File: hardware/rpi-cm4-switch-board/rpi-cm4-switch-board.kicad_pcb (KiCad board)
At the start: 2 copper layers, 114.5 x 102 mm, 68 parts, among them J1 0826-1G1T-23-F, J2 0826-1G1T-23-F, J3 0826-1G1T-23-F, P1 USB_C_Plug_USB2.0, P2 USB_C_Plug_USB2.0, U3 74LVC1G07SE-7, U5 KSZ9567RTXI, U6 AP2127N-2.5, U7 AP2127N3-1.2

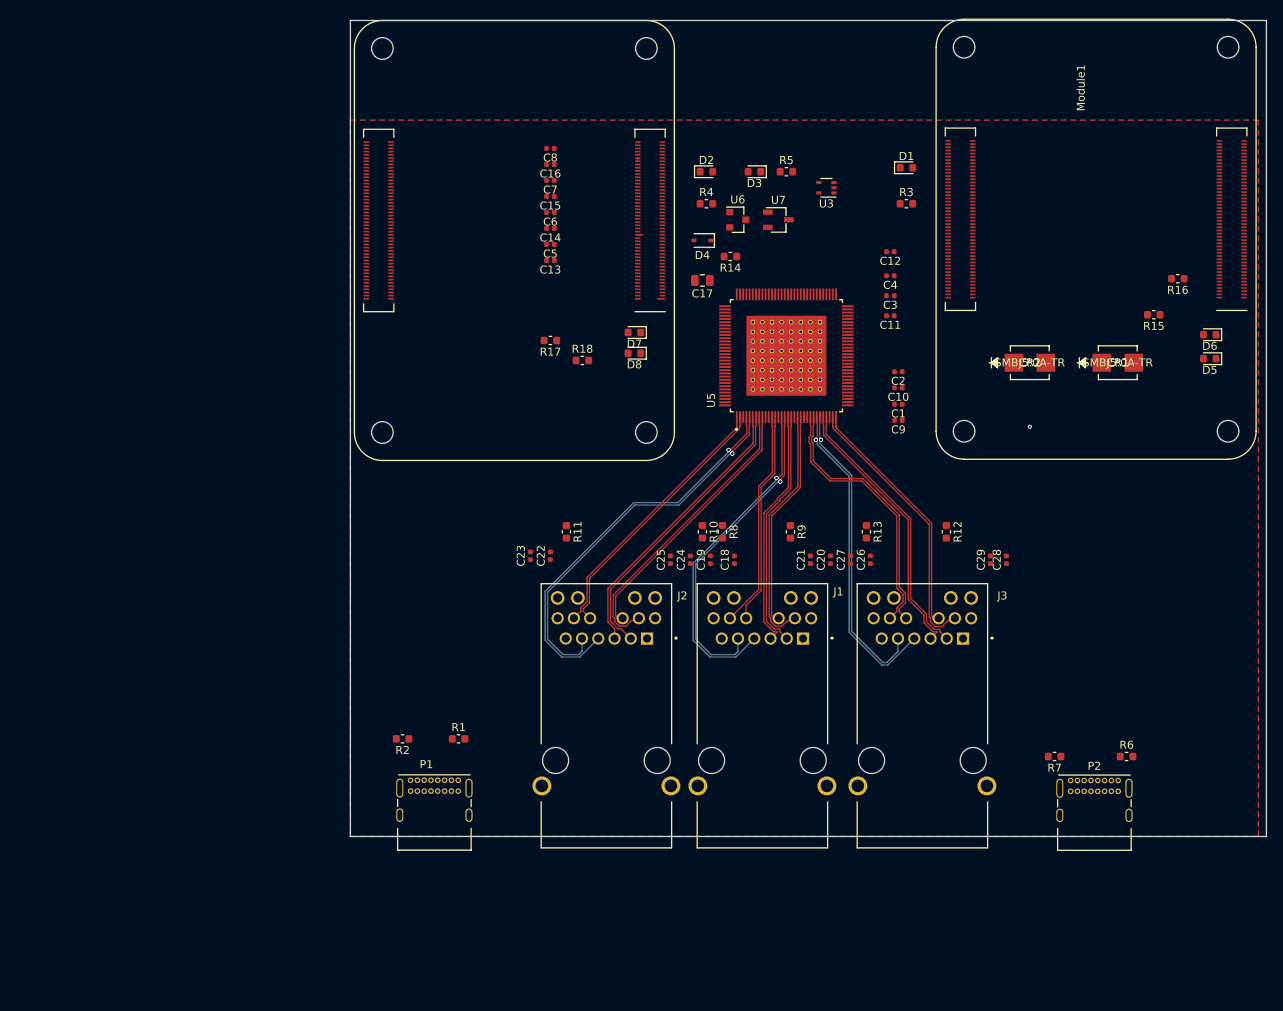
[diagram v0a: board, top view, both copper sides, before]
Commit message: Differential routing completed/roughed out. Schematic cleanup. More work to do on chip power pins.
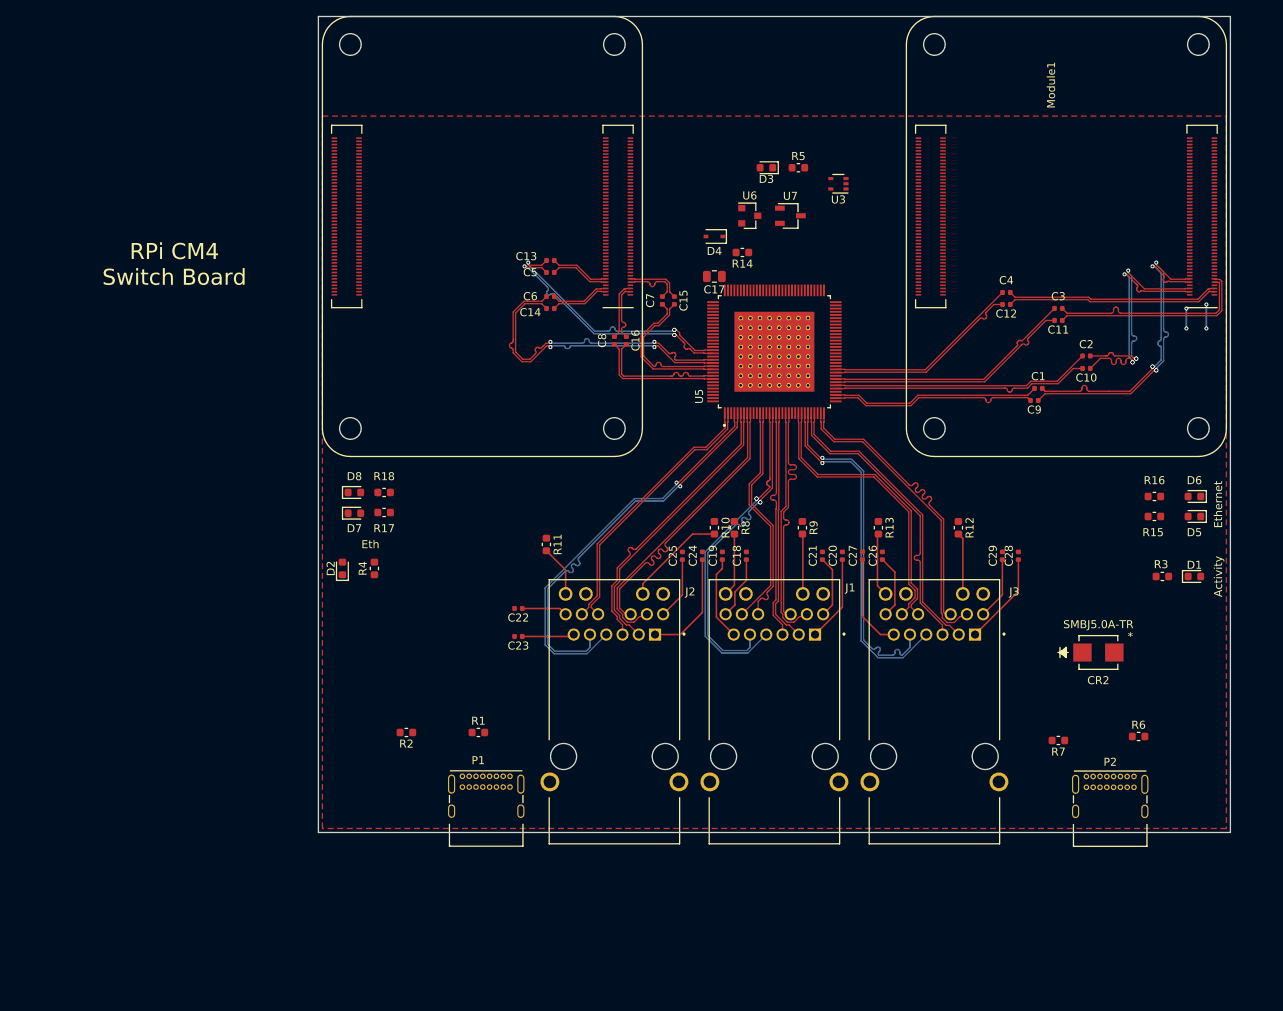
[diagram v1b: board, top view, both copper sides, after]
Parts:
- removed CR1: SMBJ5.0A-TR, footprints:SMBJ5.0A-TR
- moved D2 67.3 mm to (82.0, 113.0), turned to 90 degrees
- moved D1 62.5 mm to (188.5, 114.0)
- moved R4 61.7 mm to (86.0, 113.0), turned to 90 degrees
- moved R3 56.5 mm to (184.5, 114.0), turned to 180 degrees
- moved D7 41.7 mm to (83.5, 106.1), turned to 0 degrees
- moved D8 39.1 mm to (83.5, 103.5), turned to 0 degrees
- moved CR2 37.2 mm to (176.5, 123.5)
- moved R17 29.9 mm to (87.2, 106.0)
- moved R18 29.8 mm to (87.2, 103.5), turned to 180 degrees
- moved R16 27.4 mm to (183.5, 104.0), turned to 0 degrees
- moved C8 25.3 mm to (116.0, 84.5), turned to -90 degrees
- moved R15 25.2 mm to (183.5, 106.5), turned to 0 degrees
- moved C16 24.0 mm to (117.5, 84.5), turned to -90 degrees
- moved C10 23.6 mm to (175.0, 88.0)
- moved C2 23.6 mm to (175.0, 86.4)
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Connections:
- net Net-(C1-Pad2) renamed Cap4_A_N
- net Net-(C10-Pad2) renamed Cap4_B_P
- net Net-(C11-Pad2) renamed Cap4_C_P
- net Net-(C12-Pad2) renamed Cap4_D_P
- net Net-(C13-Pad2) renamed Cap5_A_P
- net Net-(C14-Pad2) renamed Cap5_B_P
- net Net-(C15-Pad2) renamed Cap5_C_P
- net Net-(C16-Pad2) renamed Cap5_D_P
- net Net-(C2-Pad2) renamed Cap4_B_N
- net Net-(C3-Pad2) renamed Cap4_C_N
- net Net-(C4-Pad2) renamed Cap4_D_N
- net Net-(C5-Pad2) renamed Cap5_A_N
- net Net-(C6-Pad2) renamed Cap5_B_N
- net Net-(C7-Pad2) renamed Cap5_C_N
- net Net-(C8-Pad2) renamed Cap5_D_N
- net Net-(C9-Pad2) renamed Cap4_A_P
- Module1 pad 37: /GPIO7 -> (no net)
- Module1 pad 38: /GPIO11 -> (no net)
- Module1 pad 39: /GPIO8 -> (no net)
- Module1 pad 40: /GPIO9 -> (no net)
- Module1 pad 44: /GPIO10 -> (no net)
- Module1 pad 51: /GPIO15 -> (no net)
- Module1 pad 55: /GPIO14 -> (no net)
- Module1 pad 56: /GPIO3 -> (no net)
- Module1 pad 58: /GPIO2 -> (no net)
- Module2 pad 37: /GPIO7 -> (no net)
- Module2 pad 38: /GPIO11 -> (no net)
- Module2 pad 39: /GPIO8 -> (no net)
- Module2 pad 40: /GPIO9 -> (no net)
- Module2 pad 44: /GPIO10 -> (no net)
- Module2 pad 51: /GPIO15 -> (no net)
- Module2 pad 55: /GPIO14 -> (no net)
- Module2 pad 56: /GPIO3 -> (no net)
- Module2 pad 58: /GPIO2 -> (no net)
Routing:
- net Cap5_B_N: track 0.00 -> 38.4 mm, vias 0 -> 2
- net Cap5_B_P: track 0.00 -> 38.2 mm, vias 0 -> 2
- net Eth4_A_N: track 0.00 -> 36.4 mm, vias 0 -> 3
- net Eth4_A_P: track 0.00 -> 36.4 mm, vias 0 -> 3
- net Cap4_B_N: track 0.00 -> 32.4 mm
- net Cap4_B_P: track 0.00 -> 32.4 mm
- net Cap5_A_N: track 0.00 -> 32.3 mm, vias 0 -> 3
- net Cap5_A_P: track 0.00 -> 31.5 mm, vias 0 -> 3
- net Cap4_C_N: track 0.00 -> 31.3 mm
- net Cap4_C_P: track 0.00 -> 31.1 mm
- net Eth4_B_P: track 0.00 -> 29.3 mm, vias 0 -> 3
- net Eth4_B_N: track 0.00 -> 27.4 mm, vias 0 -> 3
- net Eth4_D_N: track 0.00 -> 26.5 mm
- net Eth4_D_P: track 0.00 -> 26.4 mm
- net Cap4_A_N: track 0.00 -> 26.0 mm
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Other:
- board size 114.5 x 102 mm -> 114 x 102 mm
- board text added: "Activity"
- board text added: "Eth"
- board text added: "Ethernet"
- board text added: "RPi CM4 Switch Board"
- board text removed: "RPi CM4 LiM Carrier Board"

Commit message: Updated schematic symbol and footprint for ethernet chip, More work TBD
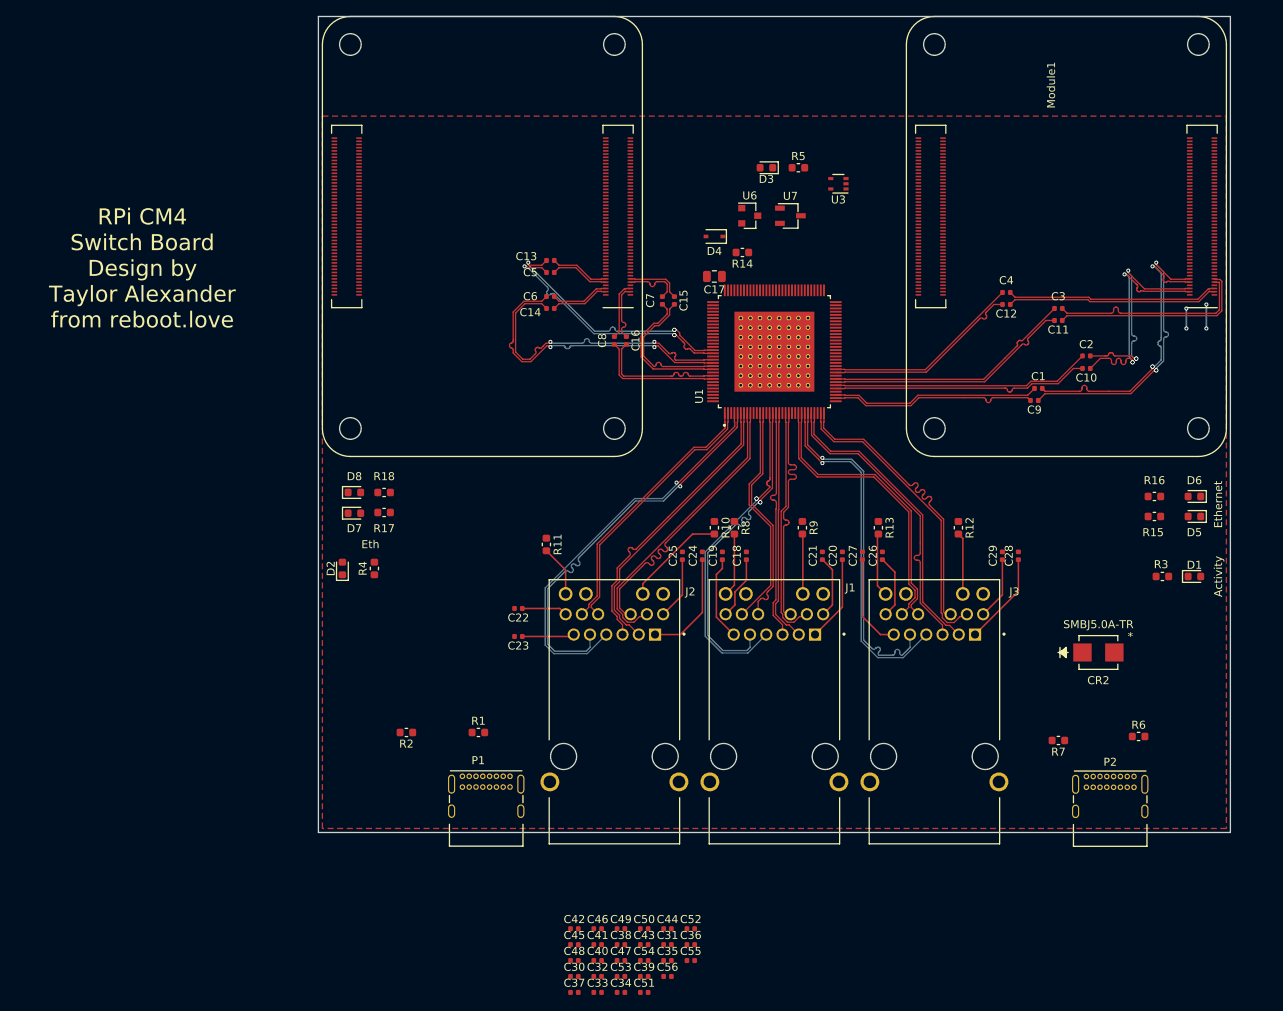
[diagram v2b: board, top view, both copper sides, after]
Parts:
- removed U5: KSZ9567RTXI, library:QFP40P1600X1600X120-129N
- added C30: 0.1uF, Capacitor_SMD:C_0402_1005Metric, F.Cu at (111.0, 164.0)
- added C31: 0.1uF, Capacitor_SMD:C_0402_1005Metric, F.Cu at (122.6, 160.0)
- added C32: 0.1uF, Capacitor_SMD:C_0402_1005Metric, F.Cu at (113.9, 164.0)
- added C33: 0.1uF, Capacitor_SMD:C_0402_1005Metric, F.Cu at (113.9, 166.0)
- added C34: 0.1uF, Capacitor_SMD:C_0402_1005Metric, F.Cu at (116.8, 166.0)
- added C35: 0.1uF, Capacitor_SMD:C_0402_1005Metric, F.Cu at (122.6, 162.0)
- added C36: 0.1uF, Capacitor_SMD:C_0402_1005Metric, F.Cu at (125.5, 160.0)
- added C37: 0.1uF, Capacitor_SMD:C_0402_1005Metric, F.Cu at (111.0, 166.0)
- added C38: 0.1uF, Capacitor_SMD:C_0402_1005Metric, F.Cu at (116.8, 160.0)
- added C39: 0.1uF, Capacitor_SMD:C_0402_1005Metric, F.Cu at (119.7, 164.0)
- added C40: 0.1uF, Capacitor_SMD:C_0402_1005Metric, F.Cu at (113.9, 162.0)
- added C41: 0.1uF, Capacitor_SMD:C_0402_1005Metric, F.Cu at (113.9, 160.0)
- added C42: 0.1uF, Capacitor_SMD:C_0402_1005Metric, F.Cu at (111.0, 158.0)
- added C43: 0.1uF, Capacitor_SMD:C_0402_1005Metric, F.Cu at (119.7, 160.0)
- added C44: 0.1uF, Capacitor_SMD:C_0402_1005Metric, F.Cu at (122.6, 158.0)
- added C45: 0.1uF, Capacitor_SMD:C_0402_1005Metric, F.Cu at (111.0, 160.0)
- added C46: 0.1uF, Capacitor_SMD:C_0402_1005Metric, F.Cu at (113.9, 158.0)
- added C47: 0.1uF, Capacitor_SMD:C_0402_1005Metric, F.Cu at (116.8, 162.0)
- added C48: 0.1uF, Capacitor_SMD:C_0402_1005Metric, F.Cu at (111.0, 162.0)
- added C49: 0.1uF, Capacitor_SMD:C_0402_1005Metric, F.Cu at (116.8, 158.0)
- added C50: 0.1uF, Capacitor_SMD:C_0402_1005Metric, F.Cu at (119.7, 158.0)
- added C51: 0.1uF, Capacitor_SMD:C_0402_1005Metric, F.Cu at (119.7, 166.0)
- added C52: 0.1uF, Capacitor_SMD:C_0402_1005Metric, F.Cu at (125.5, 158.0)
- added C53: 0.1uF, Capacitor_SMD:C_0402_1005Metric, F.Cu at (116.8, 164.0)
- added C54: 0.1uF, Capacitor_SMD:C_0402_1005Metric, F.Cu at (119.7, 162.0)
- added C55: 0.1uF, Capacitor_SMD:C_0402_1005Metric, F.Cu at (125.5, 162.0)
- added C56: 0.1uF, Capacitor_SMD:C_0402_1005Metric, F.Cu at (122.6, 164.0)
- added U1: KSZ9567S, library:QFP40P1600X1600X120-129N, F.Cu at (136.0, 85.9)
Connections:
- U6 pad 2: Net-(U5-Pad10) -> 2.5V
- U7 pad 2: Net-(U5-Pad104) -> 1.2V
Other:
- board text added: "RPi CM4 Switch Board Design by Taylor Alexander from reboot.love"
- board text removed: "RPi CM4 Switch Board"
